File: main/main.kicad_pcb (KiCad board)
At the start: 2 copper layers, 31.2 x 55.4 mm, 23 parts, among them IC1 MB1010-000, M1 Motor_DC, P1 Digital, P2 Analog, P3 CONN_01X01, P4 CONN_01X01, P5 CONN_01X01, P6 CONN_01X01, Q1 PN2222A, U1 SW_PWR_BTN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

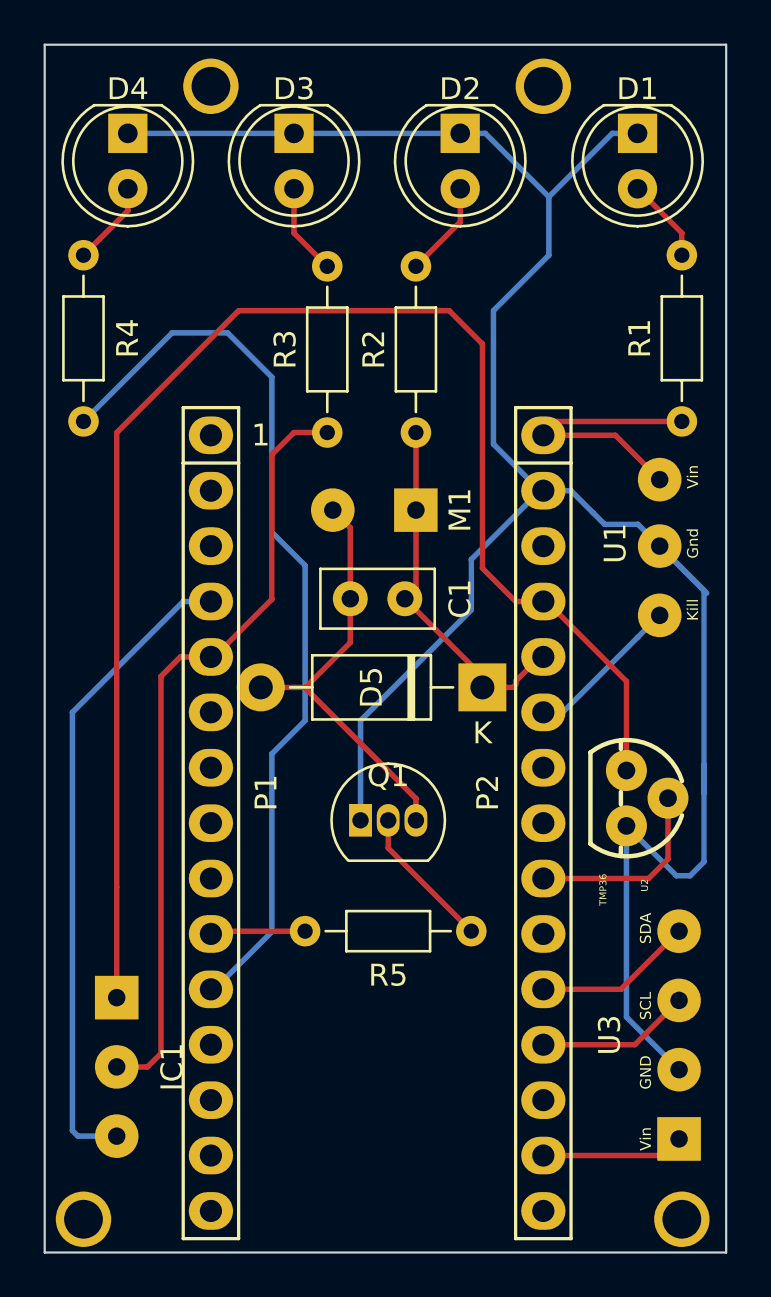
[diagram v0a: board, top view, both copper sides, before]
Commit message: pcb: Enlarged all trace widths to 0.44mm to allow printing at
E5 prototyping center
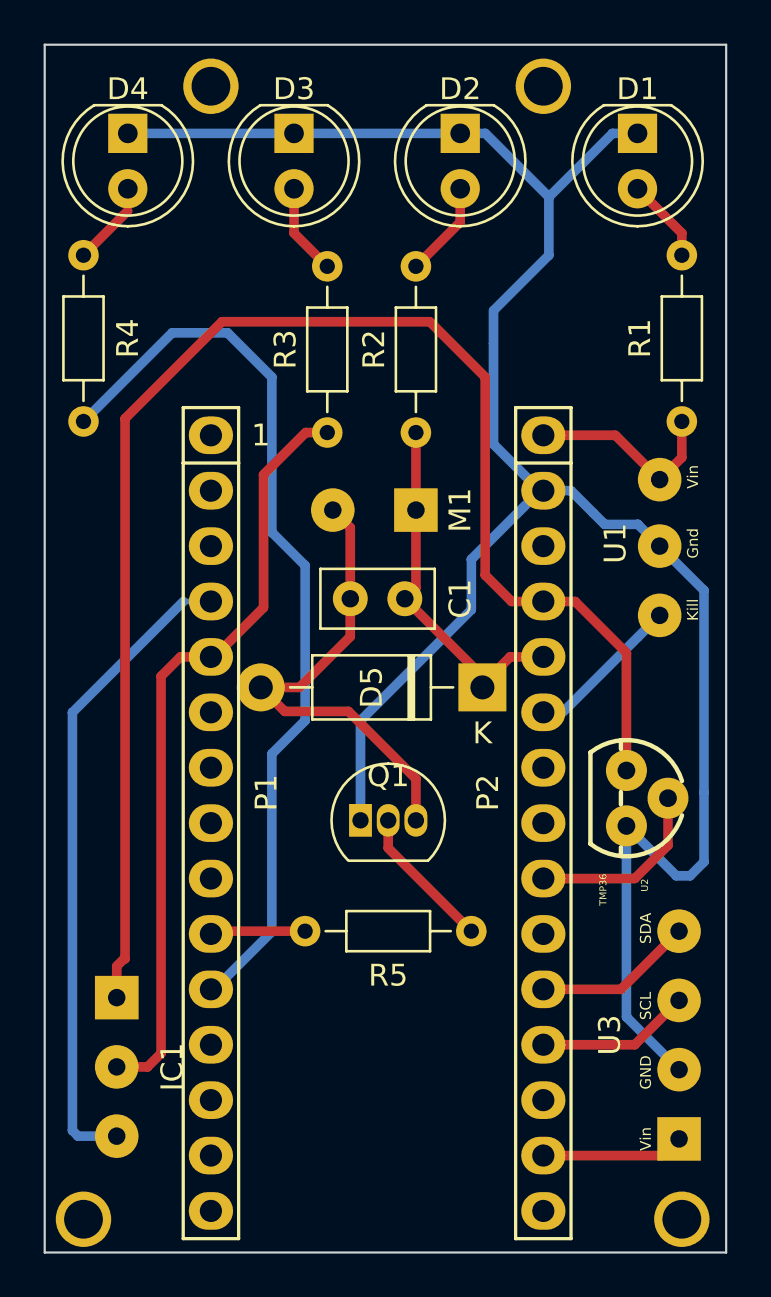
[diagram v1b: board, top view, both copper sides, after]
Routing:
- net /Vin: track 12.9 -> 9.42 mm
- net GND: track 132.6 -> 129.5 mm
- net Net-(C1-Pad2): track 19.6 -> 22.0 mm
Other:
- rule trace_min: 0.2 -> 0.44
- rule via_min_size: 0.4 -> 0.44
